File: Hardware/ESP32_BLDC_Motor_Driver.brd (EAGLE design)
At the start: 81.3 x 57.1 mm, 102 parts, among them J2 0532610371, J3 POWER_JACKPOWER_JACK_SLOT, J6 0.1in header, J7 QWIIC_RIGHT_ANGLE, Q1 20V/4.2A/52mΩ/1.4W, U1 TMC6300, U2 OPA344, U3 ESP-WROOM-3232D-NARROW, U4 CH340C, U5 ESD Diode, U6 AP63357, U7 AP2202-ADJ

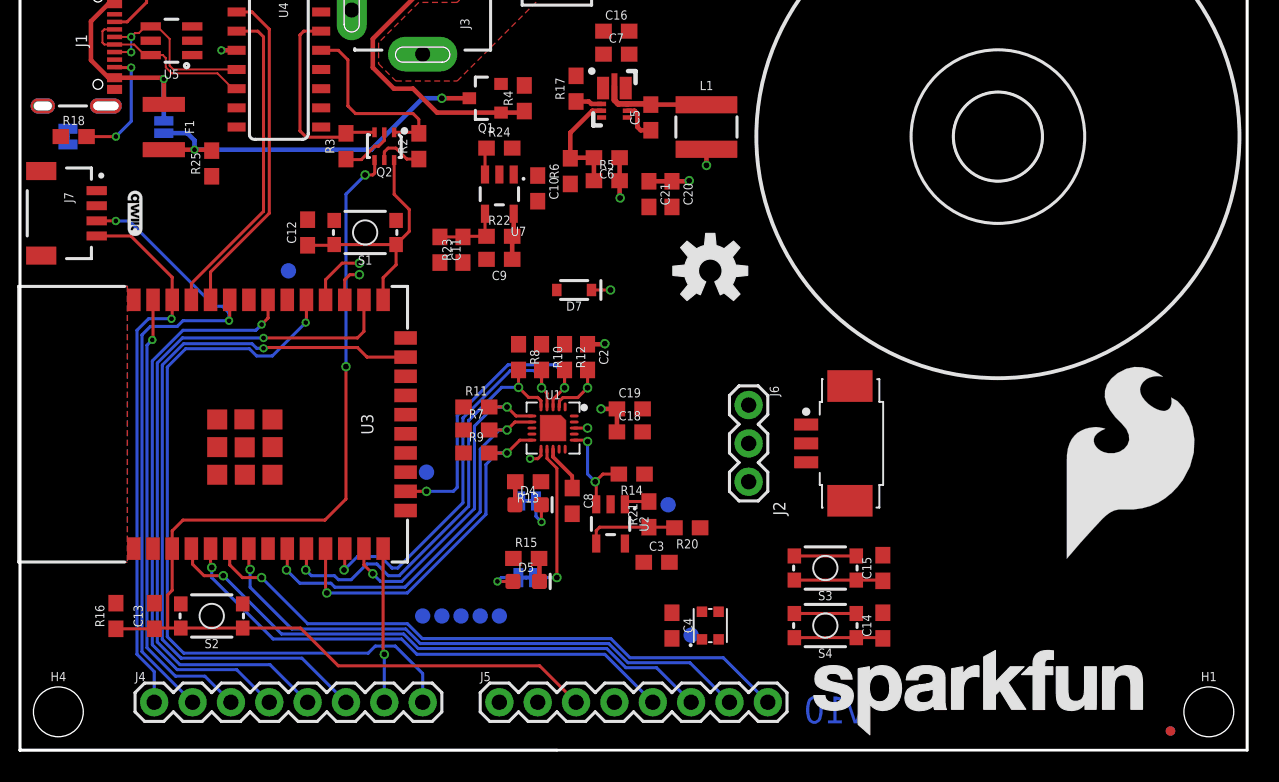
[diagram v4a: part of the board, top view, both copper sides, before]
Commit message: Updates to library and schematic
Added decoupling caps to ESP32 as per the datasheet, updated the library for the magnetic encoder for better schematic routing, moved components on the board for layout, made small changes/fixes to schematic for net label names and for the breakout header
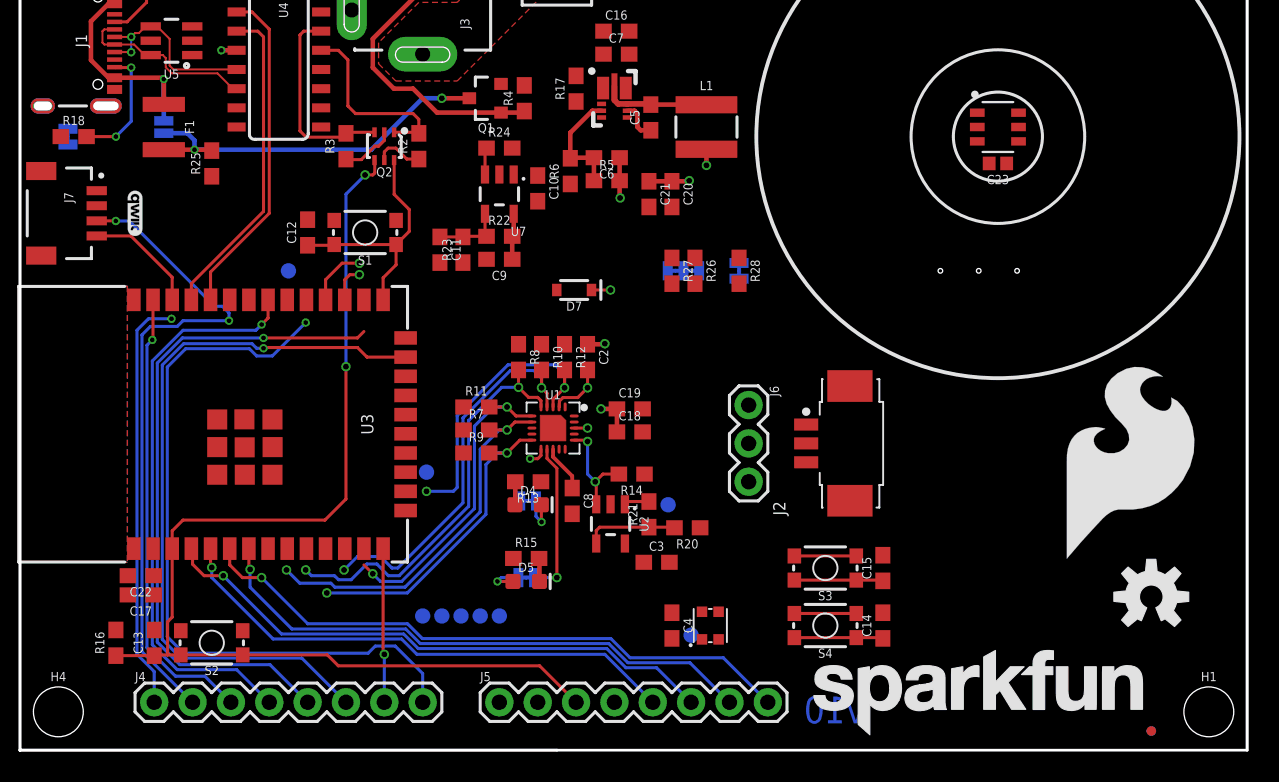
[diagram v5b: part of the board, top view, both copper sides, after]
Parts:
- added C17: 0.1uF, SparkFun-Capacitors:0603
- added C22: 22uF, SparkFun-Capacitors:0603
- added C23: 0.1uF, SparkFun-Capacitors:0402
- added I2C: JUMPER-SMT_3_2-NC_TRACE_SILK, SparkFun-Jumpers:SMT-JUMPER_3_2-NC_TRACE_SILK
- added INT: JUMPER-SMT_2_NC_TRACE_SILK, SparkFun-Jumpers:SMT-JUMPER_2_NC_TRACE_SILK
- added R26, R27: 2.2k, SparkFun-Resistors:0603
- added R28: 10k, SparkFun-Resistors:0603
- added U8: TMAG5273, TMAG5273:SOT23-6_DBV_TEX
- moved LOGO2 36.3 mm to (74.9, 10.2)
- moved FRAME1 5.08 mm to (20.3, -35.6)
- moved C13 1.78 mm to (8.89, 7.11)
- moved R16 1.78 mm to (6.35, 7.11)
- moved S2 1.78 mm to (12.7, 7.11)
- moved FD1 1.27 mm to (74.9, 1.27)
- moved FD2 1.27 mm to (74.9, 1.27)
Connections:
- net CURR_SENSE renamed ESP_32/CURR_SENSE
- net DIAG renamed ESP_18/DIAG
- net EN renamed ESP_17/EN
- net EN_MOTOR renamed ESP_16/EN_MOTOR_PWR
- net ESP_4 renamed ESP_4/GPIO4
- net ESP_5 renamed ESP_5/GPIO5
- net UH renamed ESP_13/UH
- net UL renamed ESP_14/UL
- net VH renamed ESP_27/VH
- net VL renamed ESP_26/VL
- net WH renamed ESP_25/WH
- net WL renamed ESP_33/WL
- new net !INT: R28.1, U8.5
- new net ESP_0/!STDBY: U3.24
- new net N$11: INT.1, R28.2
- new net N$12: I2C.3, R27.2
- new net N$13: I2C.1, R26.2
- net !STDBY: no longer U3.24
- net 3.3V_LDO: now also C17.1, C22.1, C23.1, I2C.2, INT.2, U8.4
- net ESP_21/TP_SDA: now also R26.1, U8.6
- net ESP_22/TP_SCL: now also R27.1, U8.1
- net GND: now also C17.2, C22.2, C23.2, U8.2, U8.3
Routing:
- net ESP_26/VL: track 23.9 -> 21.0 mm
- net ESP_4/GPIO4: track 46.7 -> 44.6 mm
- net ESP_16/EN_MOTOR_PWR: track 4.20 -> 2.44 mm
- net ESP_5/GPIO5: track 50.4 -> 48.9 mm
- net ESP_13/UH: track 20.7 -> 19.3 mm
- net ESP_33/WL: track 26.3 -> 24.9 mm
- net ESP_25/WH: track 28.5 -> 27.1 mm
- net ESP_27/VH: track 27.4 -> 26.0 mm
- net ESP_21/TP_SDA: track 45.1 -> 43.7 mm
- net ESP_22/TP_SCL: track 36.6 -> 35.4 mm
- net ESP_14/UL: track 22.1 -> 21.0 mm
- net !RESET: track 75.0 -> 76.1 mm

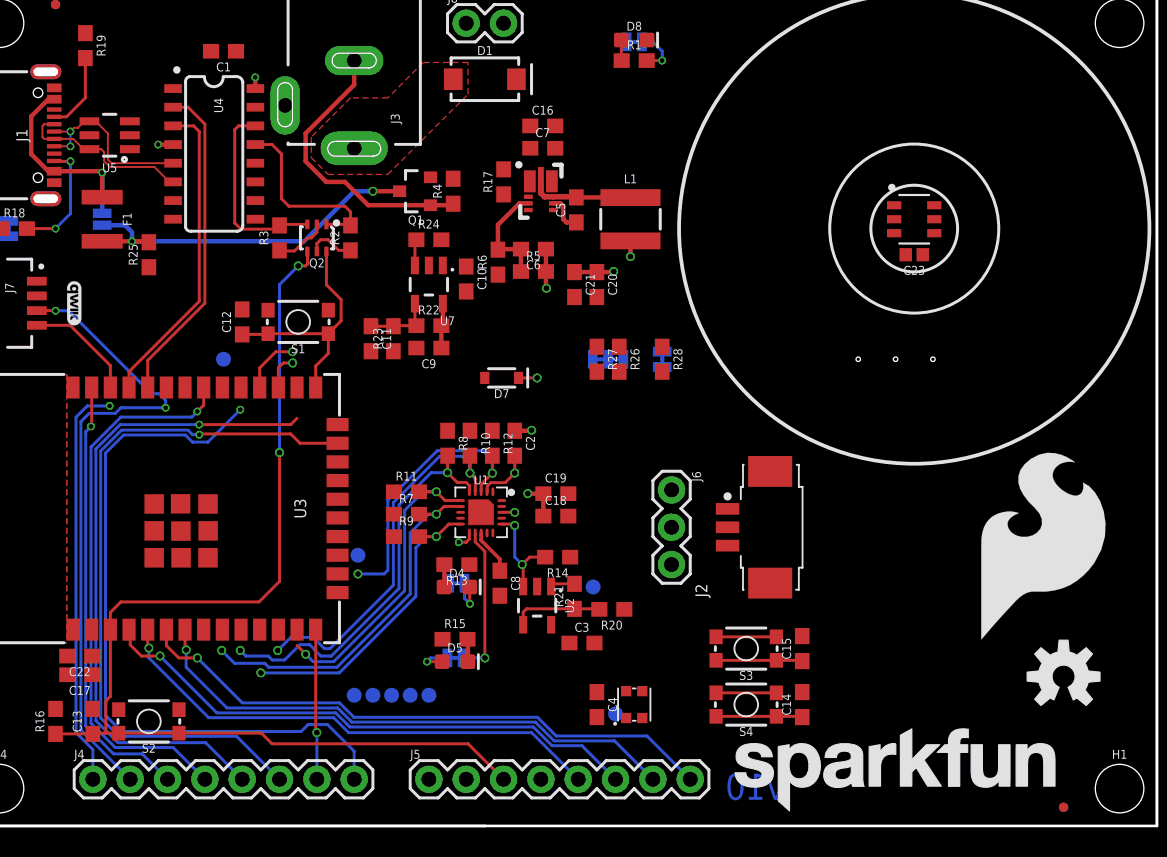
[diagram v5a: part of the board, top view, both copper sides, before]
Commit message: Design updates for board and schematic
Continued work from schematic and layout - not complete, needs more routing and placement adjustments.
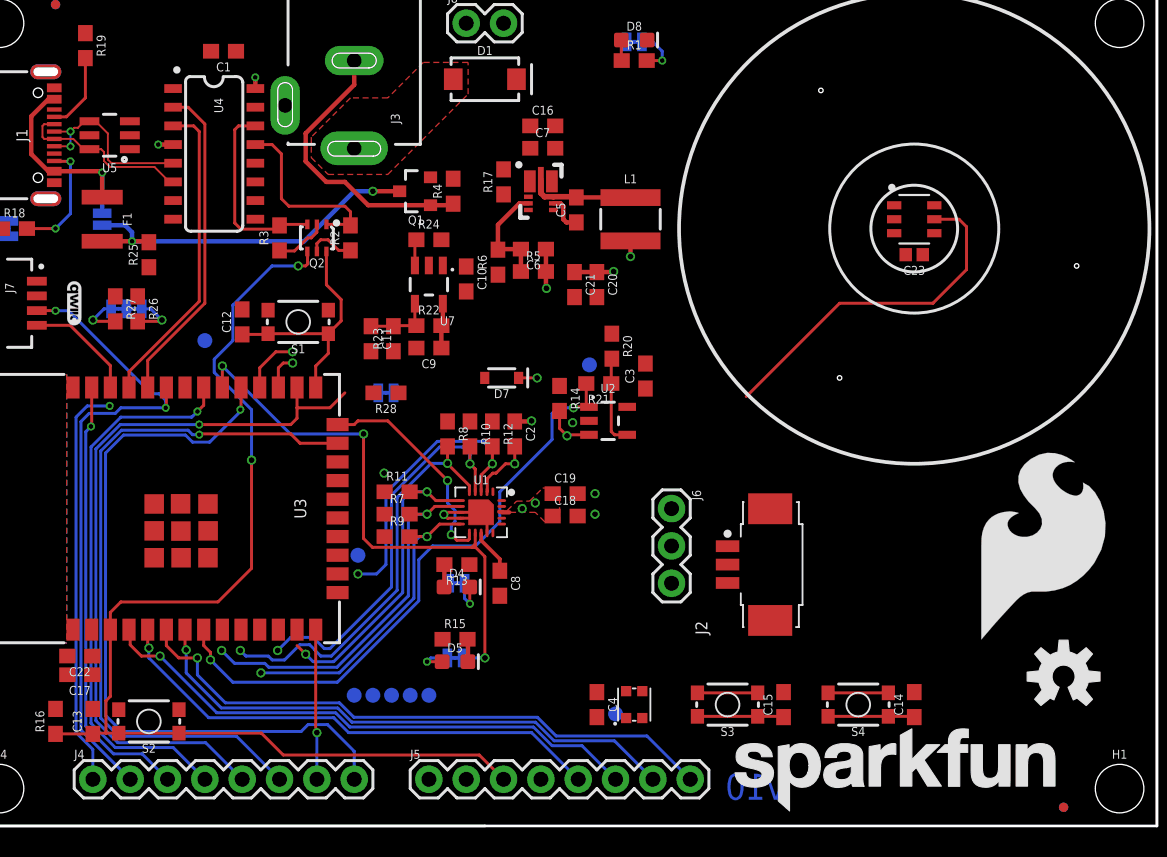
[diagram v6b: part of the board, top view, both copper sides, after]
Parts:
- moved I2C 32.9 mm to (11.2, 35.2)
- moved R26 32.9 mm to (11.9, 35.2)
- moved R27 32.9 mm to (10.4, 35.2)
- moved INT 18.9 mm to (28.8, 29.5), turned to 0 degrees
- moved R28 18.9 mm to (28.8, 29.5), turned to 180 degrees
- moved C3 18.7 mm to (46.5, 30.6), turned to 90 degrees
- moved R20 17.9 mm to (44.2, 32.6), turned to 270 degrees
- moved TP9 15.1 mm to (42.7, 31.4), turned to 270 degrees
- moved R21 14.6 mm to (43.3, 30.1), turned to 180 degrees
- moved U2 13.5 mm to (43.9, 27.6), turned to 270 degrees
- moved R14 10.8 mm to (40.6, 29.1), turned to 270 degrees
- moved FRAME1 8.52 mm to (16.5, -27.9)
- moved C14 7.62 mm to (64.8, 8.26)
- moved S4 7.62 mm to (61.0, 8.26)
- moved S3 4.02 mm to (52.1, 8.26)
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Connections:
- removed net !INT: R28.1, U8.5
- removed net !STDBY: S.2, U1.11
- removed net ESP_4/GPIO4: J4.5, U3.26
- removed net N$16: J5.2
- new net ESP_4/!INT: J4.5, R28.1, U3.26, U8.5
- net ESP_0/!STDBY: now also J5.2, S.2, U1.11
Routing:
- net ESP_4/!INT: track 0.00 -> 74.3 mm, vias 0 -> 1
- net ESP_4/GPIO4: track 44.6 -> 0.00 mm, vias 1 -> 0
- net ESP_32/CURR_SENSE: track 1.67 -> 41.9 mm, vias 0 -> 2
- net ESP_18/DIAG: track 10.3 -> 38.6 mm, vias 1 -> 3
- net ESP_0/!STDBY: track 0.00 -> 15.1 mm, vias 0 -> 2
- net GND: track 0.00 -> 6.85 mm, vias 0 -> 5
- net SENSE: track 7.09 -> 3.42 mm, vias 2 -> 1
- net N$13: track 0.00 -> 3.37 mm, vias 0 -> 1
- net N$12: track 0.00 -> 3.12 mm, vias 0 -> 1
- net 3.3V: track 12.3 -> 9.36 mm
- net ESP_5/GPIO5: track 48.9 -> 50.5 mm
- net !RESET: track 76.1 -> 77.6 mm
- net ESP_21/TP_SDA: track 43.7 -> 45.1 mm
- net ESP_27/VH: track 26.0 -> 27.3 mm
- net !STDBY: track 1.23 -> 0.00 mm, vias 1 -> 0
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- added copper zone on layer 1, net 3.3V

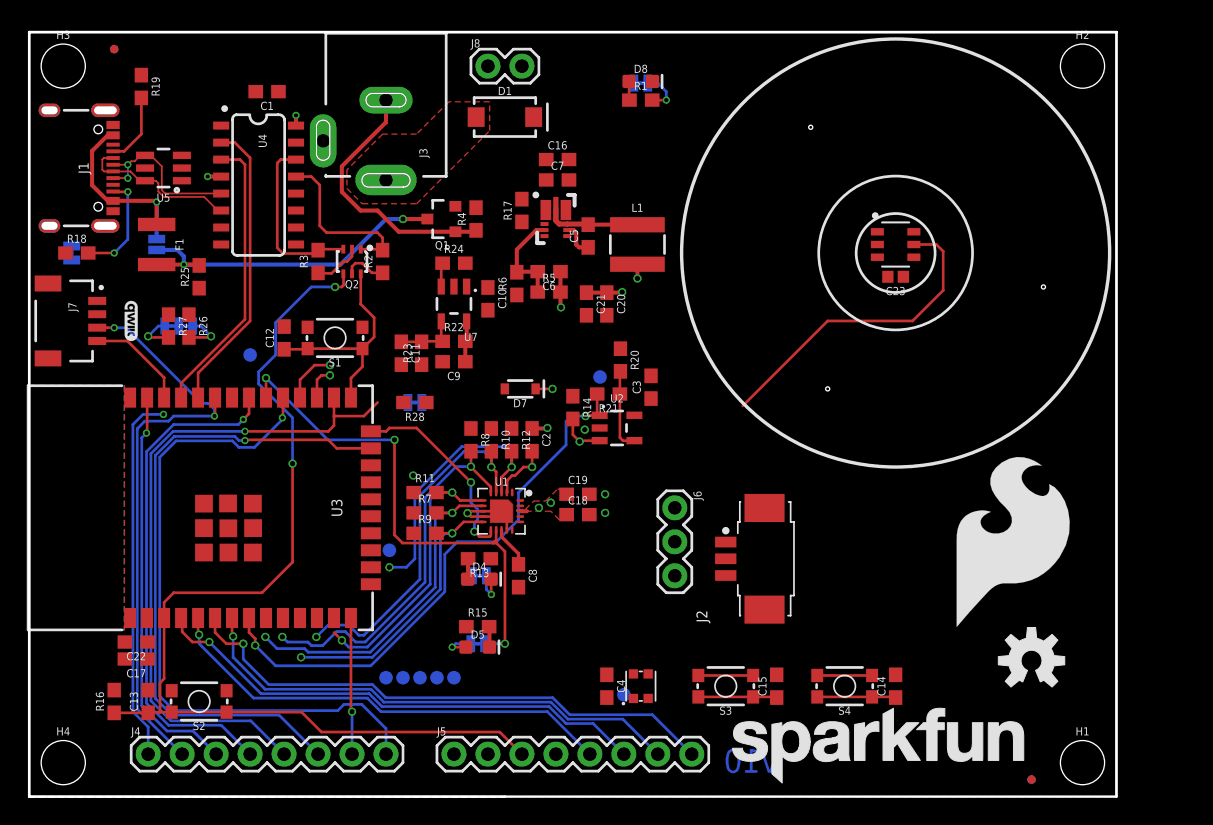
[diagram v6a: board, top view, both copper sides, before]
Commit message: Addition of motor footprint to library; updates to schematic and layout
Opened up layout of the board for addition of milling layer; broke out power good signal to the breakout headers; adjusted auxilary buttons for proper use; adjusted VIO to be configured correctly; changed note for copper weight usage; created footprint for the motor
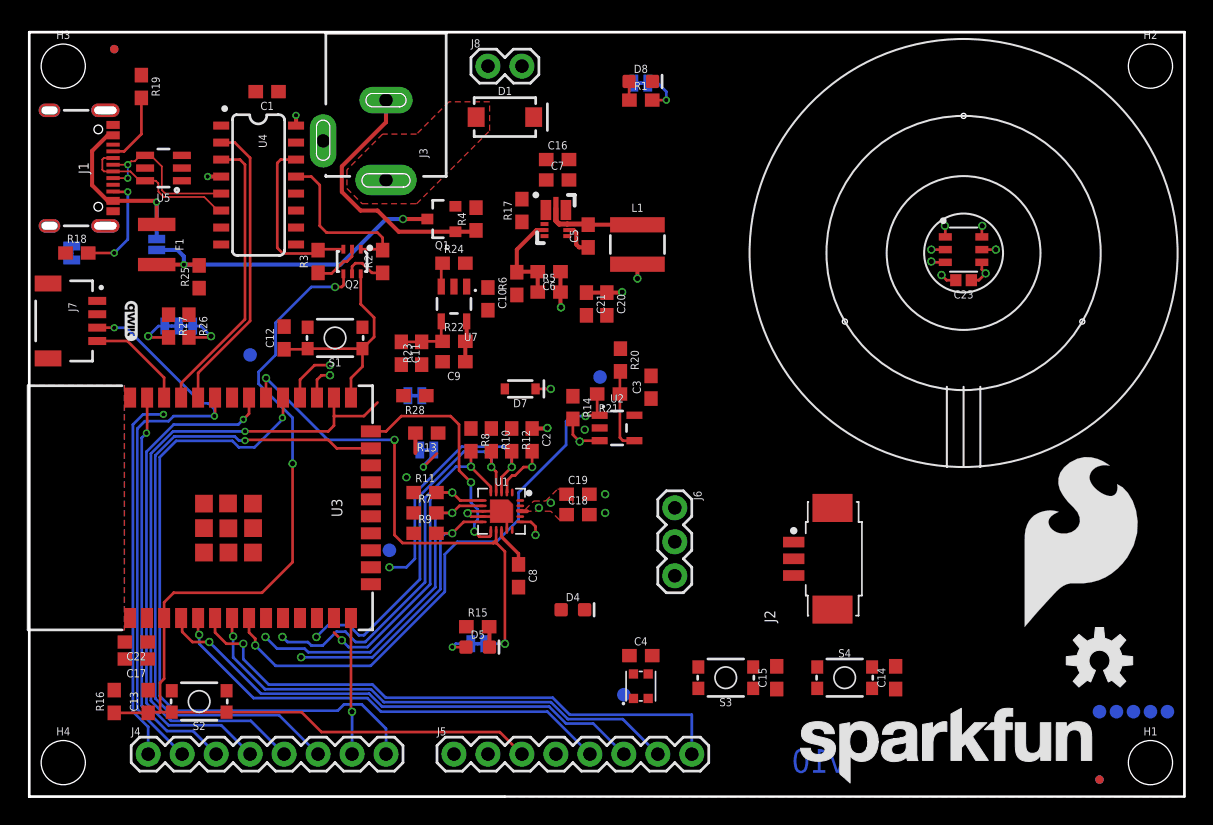
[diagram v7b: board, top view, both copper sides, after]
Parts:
- added U$2: (no value), OT-EM3215:OT-EM3215
- moved TP4 53.4 mm to (85.1, 6.35)
- moved TP7 53.4 mm to (81.3, 6.35)
- moved TP8 53.4 mm to (80.0, 6.35)
- moved TP6 53.4 mm to (82.5, 6.35)
- moved TP5 53.4 mm to (83.8, 6.35)
- moved R13 10.2 mm to (29.7, 27.2)
- moved S 10.2 mm to (29.7, 25.9)
- moved D4 7.35 mm to (40.6, 14.0)
- moved U8 5.09 mm to (69.8, 40.9)
- moved C23 5.09 mm to (69.8, 38.6)
- moved FD1 5.08 mm to (80.0, 1.27)
- moved FD2 5.08 mm to (80.0, 1.27)
- moved H1 5.08 mm to (83.8, 2.54)
- moved H2 5.08 mm to (83.8, 54.6)
- moved J2 5.08 mm to (57.1, 17.8)
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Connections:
- removed net N$10: C14.1, S4.3, S4.4
- removed net N$18: J5.1
- removed net N$9: C15.1, S3.3, S3.4
- new net 3.3V_PG: J5.1, U6.P$5
- net ESP_34/AUX1: now also C14.1, S4.3, S4.4; no longer S4.1, S4.2
- net ESP_35/AUX2: now also C15.1, S3.3, S3.4; no longer S3.1, S3.2
- net GND: now also S3.1, S3.2, S4.1, S4.2
- net N$29: now also D4.C; no longer D4.A
- net S: now also D4.A; no longer D4.C
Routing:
- net ESP_4/!INT: track 74.3 -> 51.5 mm, vias 1 -> 2
- net N$10: track 5.88 -> 0.00 mm
- net N$9: track 5.88 -> 0.00 mm
- net ESP_35/AUX2: track 41.8 -> 37.8 mm
- net GND: track 6.85 -> 10.2 mm, vias 5 -> 8
- net ESP_0/!STDBY: track 15.1 -> 17.9 mm
- net ESP_34/AUX1: track 45.3 -> 43.0 mm
- net 3.3V_LDO: track 4.83 -> 7.06 mm, vias 2 -> 3
- net SENSE: track 3.42 -> 5.34 mm, vias 1 -> 2
- net ESP_22/TP_SCL: track 35.4 -> 36.2 mm, vias 1 -> 2
- net ESP_21/TP_SDA: track 45.1 -> 45.9 mm, vias 2 -> 3
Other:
- board size 81.3 x 57.1 mm -> 86.4 x 57.1 mm
- board text added: "Board thickness is 1.6mm 4-Layer 1oz copper outer 0.5oz copper inner"
- board text removed: "Board thickness is 1.6mm 4-Layer 1oz copper outer 1oz copper inner"
